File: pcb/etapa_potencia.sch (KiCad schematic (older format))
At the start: 55 parts, among them Q1 PNP, Q10 NPN, Q11 NPN, Q12 NPN, Q13 NPN, Q14 NPN, Q15 PNP, Q16 NPN, Q17 NPN, Q18 NPN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

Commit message: subo cosas del kicad
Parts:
- removed Q14, Q18, Q?: NPN, symbol NPN
- added C10, C11, C12, C13, C5, C6, C7, C8, C9: C, symbol C
- added L1: INDUCTOR, symbol INDUCTOR
- added P? (x5): CONNECTOR, symbol CONNECTOR
- added Q14: MPSA56, symbol PNP
- added Q18: MJE350, symbol PNP
- added Q21: 2SA1302, symbol PNP
- added R21, R22, R25, R26, R27, R28, R29, R30, R31, R32, R33: R, symbol R
- Q1, Q3, Q5, Q7, Q9: value PNP -> MPSA56
- Q10, Q11, Q2, Q4, Q6, Q8: value NPN -> MPSA06
- Q12, Q13: value NPN -> MJE340
- Q15: value PNP -> MJE350
- Q16, Q17: value NPN -> 2sc3281
- Q19: value PNP -> 2SA1302
- Q20: renamed from Q?; value NPN -> MPSA06
- gave numbers to parts that had none: 4
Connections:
- net GND: now also R11.2, C10.2, C11.2, C12.2, C13.1, C5.2, C6.1, C7.2, P?.1 (W), R26.2; no longer R1.2, R6.2
- net Salida: now also L1.2, R33.2; no longer Q20.1 (E), R14.2, R15.1, R17.2, R18.1
- net at Q7.3 (C), Q9.2 (B), R6.1: now also R25.2; no longer Q3.2 (B)
- net at Q12.3 (C), Q16.3 (C), Q7.1 (E)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: now also C6.2, C8.2, C9.2, P?.1 (W), R21.1
- net at Q2.1 (E), Q4.1 (E), Q6.1 (E)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: now also C10.1, C7.1, R31.1; no longer Q15.3 (C), Q19.3 (C)
- net at Q19.1 (E): now also Q21.3 (C)
- net at D6.2 (K), R16.1: now also Q18.3 (C)
- net at C2.1, D2.2 (K), Q11.1 (E)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: now also R30.2; no longer D8.1 (A)
- net at R15.2: now also Q18.1 (E), Q21.2 (B)
- net at R18.2, R24.1: now also Q21.1 (E)
- net at D1.1 (A): now also R27.2, R28.2, R29.1; no longer Q11.3 (C)
- net at Q11.2 (B), R12.1: now also C2.2, R28.1; no longer R11.2
- net at D5.1 (A): now also P?.1 (W)
- net at D6.1 (A): now also P?.1 (W)
- net at Q20.2 (B), R23.1: now also R21.2
- net at R24.2: now also Q14.2 (B), R22.2
- net at D8.2 (K): now also Q18.2 (B), R30.1
- new net: C5.1, R1.2, R11.1
- new net: C8.1, Q3.2 (B), R25.1
- new net: C11.1, C12.1, P?.1 (W), Q15.3 (C), Q19.3 (C), R22.1, R31.2
- new net: L1.1, Q14.1 (E), Q20.1 (E), R14.2, R15.1, R17.2, R18.1, R32.1, R33.1
- new net: D1.2 (K), D3.1 (A), Q9.3 (C)
- new net: C9.1, R26.1, R6.2
- new net: Q11.3 (C), R27.1
- new net: D7.1 (A), Q13.2 (B), R29.2
- new net: D8.1 (A), Q14.3 (C)
- new net: C13.2, R32.2
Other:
- moved on the sheet: C1, C2, D1, D2, D3, D4, D5, D6, D7, D8, Q1, Q10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

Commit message: mas cosas del kicad
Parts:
- added Q22, Q23: MPSA56, symbol PNP
- added entrada1, salida1: CONNECTOR, symbol CONNECTOR
- D3, D4, D5, D6, D8: value DIODE -> 1N5819
- D7: value DIODE -> LEDRED
- gave numbers to parts that had none: 5
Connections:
- net Entrada: now also Q22.2 (B)
- net Salida: now also salida1.1 (W)
- net entrada_negativa: now also Q23.2 (B)
- net at Q1.1 (E), R2.2: now also Q22.1 (E)
- net at C1.1, Q1.3 (C), Q2.3 (C)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: now also Q22.3 (C)
- net at Q5.1 (E), R5.2: now also Q23.1 (E)
- net at Q2.2 (B), Q4.2 (B), Q4.3 (C)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: now also Q23.3 (C)
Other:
- moved on the sheet: -25V1, -50V1, 25V1, 50V1, C1, C10, C11, C12, C13, C2, C3, C4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

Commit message: kicad new
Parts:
- added C14: C, symbol C
- added R34, R35: R, symbol R
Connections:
- net Entrada: now also entrada1.1 (W), C14.1; no longer Q1.2 (B), Q22.2 (B), R1.1
- net at C10.1, C7.1, Q6.1 (E)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: now also R34.2, R35.2; no longer Q2.1 (E), Q4.1 (E)
- new net: C14.2, Q1.2 (B), Q22.2 (B), R1.1
- new net: Q4.1 (E), R35.1
- new net: Q2.1 (E), R34.1
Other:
- moved on the sheet: entrada1
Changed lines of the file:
@@
-EESchema Schematic File Version 2  date dom 29 abr 2012 23:24:54 ART
+EESchema Schematic File Version 2  date mar 01 may 2012 15:43:33 ART
 LIBS:power
 LIBS:device
@@
 Sheet 1 1
 Title ""
-Date "30 apr 2012"
+Date "1 may 2012"
 Rev ""
 Comp ""
@@
 $EndDescr
 $Comp
-L CONNECTOR entrada1
-U 1 1 4F9DF78B
-P 1150 5100
-F 0 "entrada1" V 1450 5350 70  0000 C CNN
-F 1 "CONNECTOR" V 1700 5100 70  0000 C CNN
-	1    1150 5100
-	0    -1   -1   0
-$EndComp
+L R R34
+U 1 1 4FA02EAA
+P 1700 6650
+F 0 "R34" H 1600 6700 50  0000 C CNN
+F 1 "R" H 1600 6600 50  0000 C CNN
+	1    1700 6650
+	1    0    0    -1
+$EndComp
+$Comp
+L R R35
+U 1 1 4FA02EA8
+P 2350 6650
+F 0 "R35" H 2250 6700 50  0000 C CNN
+F 1 "R" H 2250 6600 50  0000 C CNN
+	1    2350 6650
+	1    0    0    -1
+$EndComp
+Connection ~ 800  5100
+Wire Wire Line
+	800  5100 650  5100
 Connection ~ 8150 3550
 Wire Wire Line
@@
 Wire Wire Line
 	3600 6350 3600 5950
-Wire Wire Line
-	1700 6400 1700 6900
-Wire Wire Line
-	2350 6400 2350 6900
 Connection ~ 2000 3700
 Wire Wire Line
@@
 Wire Wire Line
 	1700 3700 1700 3800
-Wire Wire Line
-	1400 5100 1000 5100
 Wire Wire Line
 	2000 1650 2000 1750
@@
 Connection ~ 3100 4900
 Connection ~ 8300 3350
+Wire Wire Line
+	1400 5100 1200 5100
+$Comp
+L C C14
+U 1 1 4FA02E29
+P 1000 5100
+F 0 "C14" V 1050 5200 50  0000 L CNN
+F 1 "C" V 1050 5000 50  0000 L CNN
+	1    1000 5100
+	0    -1   -1   0
+$EndComp
+$Comp
+L CONNECTOR entrada1
+U 1 1 4F9DF78B
+P 800 5100
+F 0 "entrada1" V 1250 5050 70  0000 C CNN
+F 1 "CONNECTOR" V 1350 5100 70  0000 C CNN
+	1    800  5100
+	0    -1   -1   0
+$EndComp
 $Comp
 L CONNECTOR salida1
@@
 $EndComp
 $Comp
-L GND #PWR01
+L GND #PWR1
 U 1 1 4F9DB305
 P 1100 6350
-F 0 "#PWR01" H 1100 6350 30  0001 C CNN
+F 0 "#PWR1" H 1100 6350 30  0001 C CNN
 F 1 "GND" H 1100 6280 30  0001 C CNN
 	1    1100 6350
@@
 $EndComp
 $Comp
-L GND #PWR02
+L GND #PWR2
 U 1 1 4F9DB2D9
 P 1400 6450
-F 0 "#PWR02" H 1400 6450 30  0001 C CNN
+F 0 "#PWR2" H 1400 6450 30  0001 C CNN
 F 1 "GND" H 1400 6380 30  0001 C CNN
 	1    1400 6450
@@
 $EndComp
 $Comp
-L GND #PWR03
+L GND #PWR5
 U 1 1 4F9DAE13
 P 3150 3150
-F 0 "#PWR03" H 3150 3150 30  0001 C CNN
+F 0 "#PWR5" H 3150 3150 30  0001 C CNN
 F 1 "GND" H 3150 3080 30  0001 C CNN
 	1    3150 3150
@@
 $EndComp
 $Comp
-L GND #PWR04
+L GND #PWR3
 U 1 1 4F9DAC4C
 P 1600 1550
-F 0 "#PWR04" H 1600 1550 30  0001 C CNN
+F 0 "#PWR3" H 1600 1550 30  0001 C CNN
 F 1 "GND" H 1600 1480 30  0001 C CNN
 	1    1600 1550
@@
 $EndComp
 $Comp
-L GND #PWR05
+L GND #PWR4
 U 1 1 4F9DAB03
 P 1700 7300
-F 0 "#PWR05" H 1700 7300 30  0001 C CNN
+F 0 "#PWR4" H 1700 7300 30  0001 C CNN
 F 1 "GND" H 1700 7230 30  0001 C CNN
 	1    1700 7300
@@
 $EndComp
 $Comp
-L GND #PWR06
+L GND #PWR7
 U 1 1 4F9DAB00
 P 4100 7300
-F 0 "#PWR06" H 4100 7300 30  0001 C CNN
+F 0 "#PWR7" H 4100 7300 30  0001 C CNN
 F 1 "GND" H 4100 7230 30  0001 C CNN
 	1    4100 7300
@@
 $EndComp
 $Comp
-L GND #PWR07
+L GND #PWR8
 U 1 1 4F9DAAF8
 P 5350 7300
-F 0 "#PWR07" H 5350 7300 30  0001 C CNN
+F 0 "#PWR8" H 5350 7300 30  0001 C CNN
 F 1 "GND" H 5350 7230 30  0001 C CNN
 	1    5350 7300
@@
 $EndComp
 $Comp
-L GND #PWR08
+L GND #PWR9
 U 1 1 4F9DAA9E
 P 6250 7300
-F 0 "#PWR08" H 6250 7300 30  0001 C CNN
+F 0 "#PWR9" H 6250 7300 30  0001 C CNN
 F 1 "GND" H 6250 7230 30  0001 C CNN
 	1    6250 7300
@@
 $EndComp
 $Comp
-L GND #PWR09
+L GND #PWR10
 U 1 1 4F9DA90A
 P 7000 4500
-F 0 "#PWR09" H 7000 4500 30  0001 C CNN
+F 0 "#PWR10" H 7000 4500 30  0001 C CNN
 F 1 "GND" H 7000 4430 30  0001 C CNN
 	1    7000 4500
@@
 $EndComp
 $Comp
-L PWR_FLAG #FLG010
+L PWR_FLAG #FLG2
 U 1 1 4F9825A9
 P 6850 6900
-F 0 "#FLG010" H 6850 6995 30  0001 C CNN
+F 0 "#FLG2" H 6850 6995 30  0001 C CNN
 F 1 "PWR_FLAG" H 6850 7080 30  0000 C CNN
 	1    6850 6900
@@
 $EndComp
 $Comp
-L GND #PWR011
+L GND #PWR12
 U 1 1 4F983192
 P 10300 2300
-F 0 "#PWR011" H 10300 2300 30  0001 C CNN
+F 0 "#PWR12" H 10300 2300 30  0001 C CNN
 F 1 "GND" H 10300 2230 30  0001 C CNN
 	1    10300 2300
@@
 $EndComp
 $Comp
-L PWR_FLAG #FLG012
+L PWR_FLAG #FLG5
 U 1 1 4F98318F
 P 10300 2300
-F 0 "#FLG012" H 10300 2395 30  0001 C CNN
+F 0 "#FLG5" H 10300 2395 30  0001 C CNN
 F 1 "PWR_FLAG" H 10300 2480 30  0000 C CNN
 	1    10300 2300
@@
 $EndComp
 $Comp
-L GND #PWR013
+L GND #PWR11
 U 1 1 4F9830FE
 P 9400 2900
-F 0 "#PWR013" H 9400 2900 30  0001 C CNN
+F 0 "#PWR11" H 9400 2900 30  0001 C CNN
 F 1 "GND" H 9400 2830 30  0001 C CNN
 	1    9400 2900
@@
 $EndComp
 $Comp
-L PWR_FLAG #FLG014
+L PWR_FLAG #FLG4
 U 1 1 4F9825F5
 P 7250 5250
-F 0 "#FLG014" H 7250 5345 30  0001 C CNN
+F 0 "#FLG4" H 7250 5345 30  0001 C CNN
 F 1 "PWR_FLAG" H 7250 5430 30  0000 C CNN
 	1    7250 5250
@@
 $EndComp
 $Comp
-L PWR_FLAG #FLG015
+L PWR_FLAG #FLG1
 U 1 1 4F982566
 P 6800 1150
-F 0 "#FLG015" H 6800 1245 30  0001 C CNN
+F 0 "#FLG1" H 6800 1245 30  0001 C CNN
 F 1 "PWR_FLAG" H 6800 1330 30  0000 C CNN
 	1    6800 1150
@@
 $EndComp
 $Comp
-L PWR_FLAG #FLG016
+L PWR_FLAG #FLG3
 U 1 1 4F98250E
 P 7050 2050
-F 0 "#FLG016" H 7050 2145 30  0001 C CNN
+F 0 "#FLG3" H 7050 2145 30  0001 C CNN
 F 1 "PWR_FLAG" H 7050 2230 30  0000 C CNN
 	1    7050 2050
@@
 U 1 1 4F981666
 P 3850 5300
-F 0 "C1" H 3900 5400 50  0000 L CNN
-F 1 "C" H 3900 5200 50  0000 L CNN
+F 0 "C1" V 3900 5400 50  0000 L CNN
+F 1 "C" V 3900 5200 50  0000 L CNN
 	1    3850 5300
 	0    -1   -1   0
@@
 $EndComp
 $Comp
-L GND #PWR017
+L GND #PWR6
 U 1 1 4F9810F5
 P 3750 5500
-F 0 "#PWR017" H 3750 5500 30  0001 C CNN
+F 0 "#PWR6" H 3750 5500 30  0001 C CNN
 F 1 "GND" H 3750 5430 30  0001 C CNN
 	1    3750 5500
@@
 	1    0    0    1
 $EndComp
-Text GLabel 1000 5100 0    60   Input ~ 0
+Text GLabel 650  5100 0    60   Input ~ 0
 Entrada
 $Comp

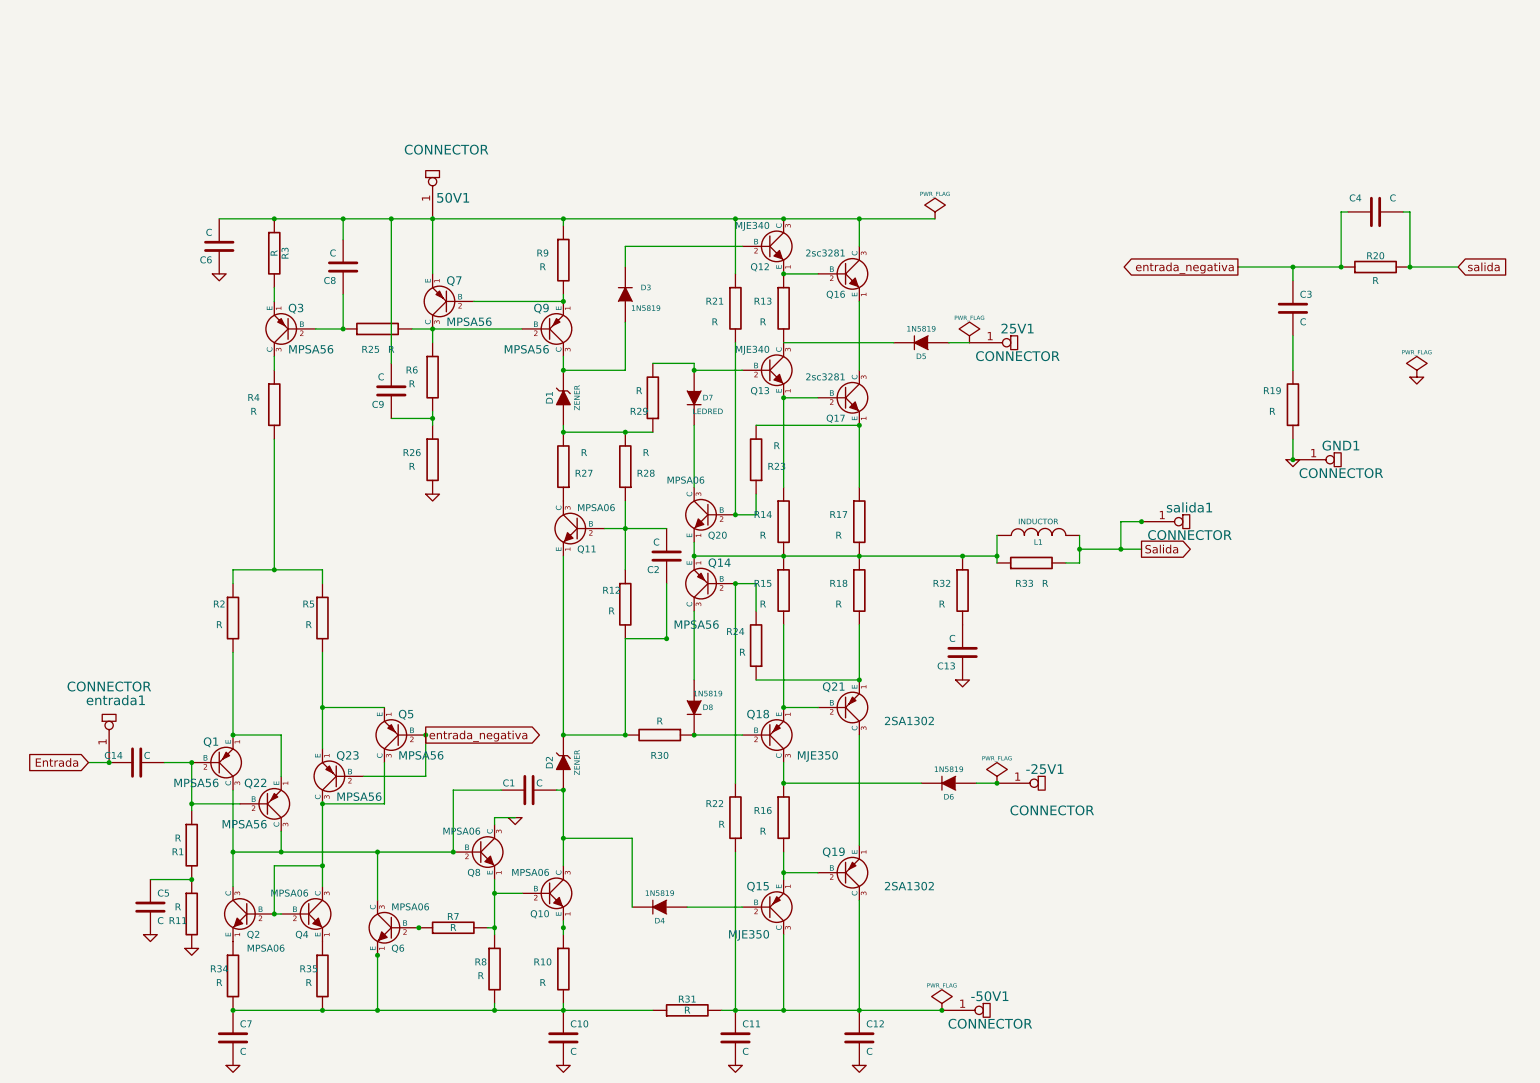
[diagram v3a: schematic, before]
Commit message: 
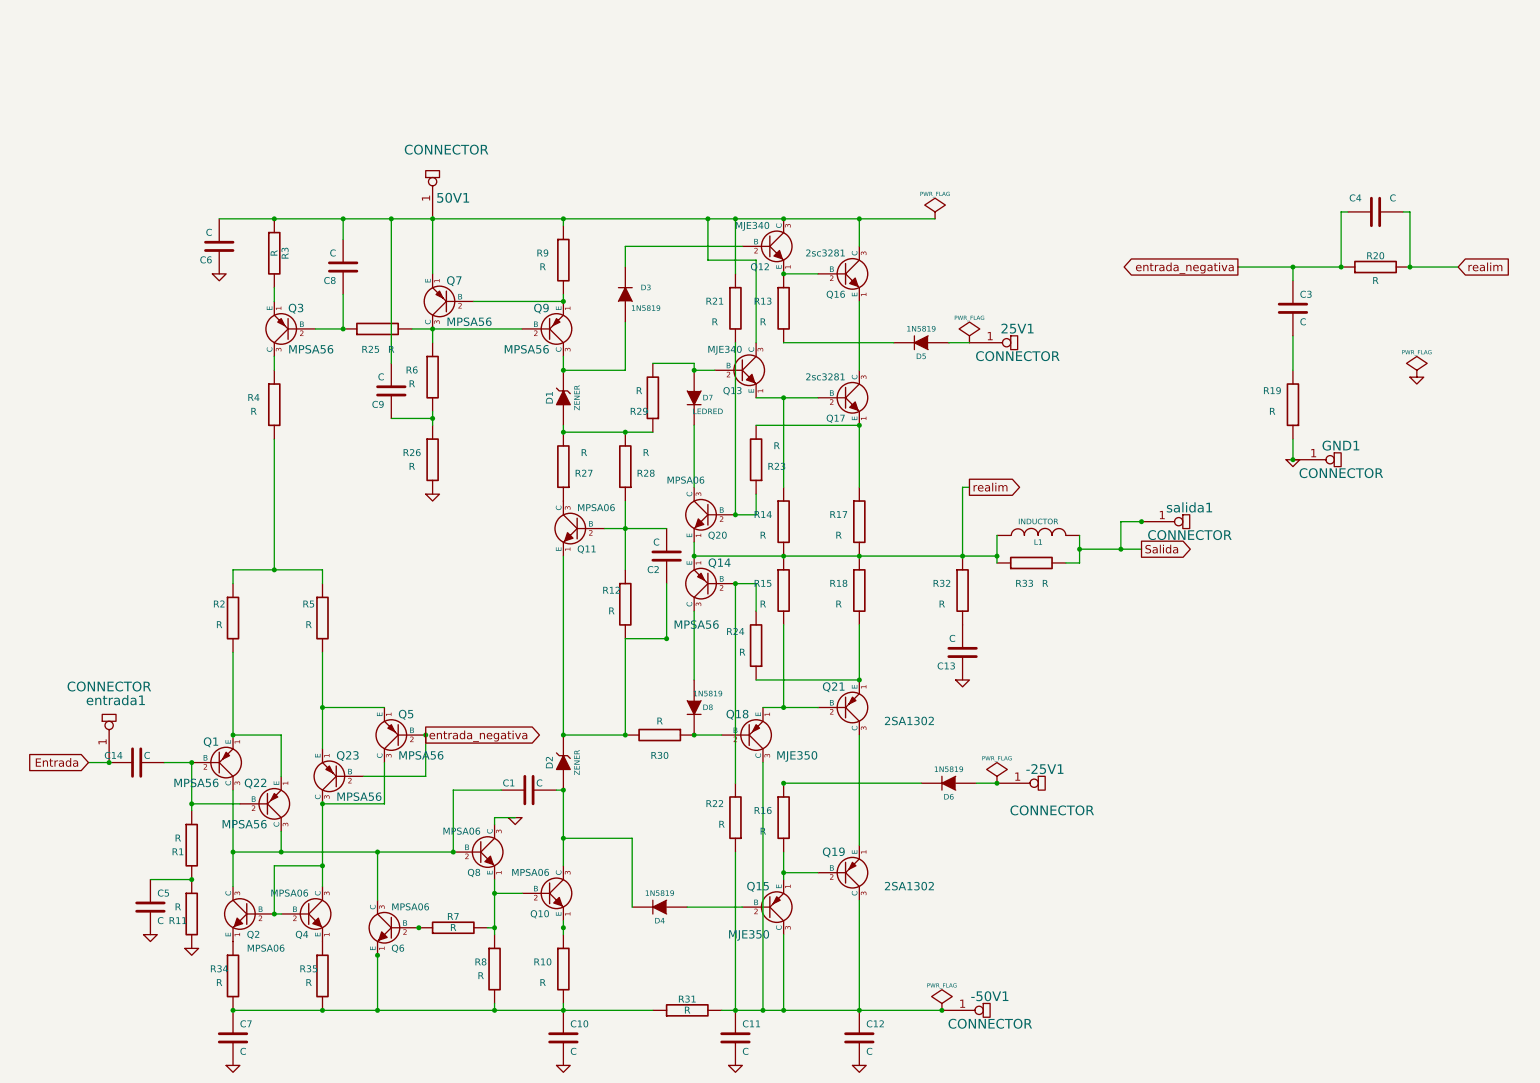
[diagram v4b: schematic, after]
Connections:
- net salida is gone; now on net realim: C4.2, R20.2
- net at 50V1.1 (W), C6.2, C8.2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: now also Q13.3 (C)
- net at -50V1.1 (W), C11.1, C12.1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: now also Q18.3 (C)
- net at D6.2 (K), R16.1: no longer Q18.3 (C)
- net realim: now reaches L1.1, Q14.1 (E), Q20.1 (E), R14.2, R15.1, R17.2, R18.1, R32.1, R33.1
- net at D5.2 (K), R13.2: no longer Q13.3 (C)
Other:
- moved on the sheet: Q13, Q18
